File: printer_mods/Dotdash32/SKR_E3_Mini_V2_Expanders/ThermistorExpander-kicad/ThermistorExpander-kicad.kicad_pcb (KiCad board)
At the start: 2 copper layers, 20.5 x 21.8 mm, 8 parts, among them J1 SPI_Header, J2 JST-XH2, J3 JST-XH2, J4 JST-XH2

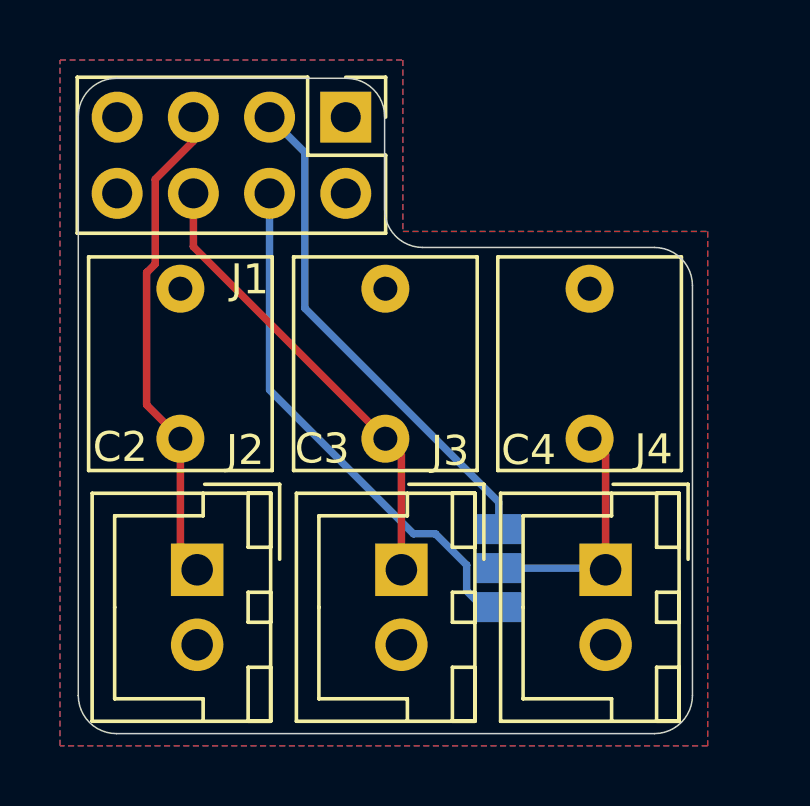
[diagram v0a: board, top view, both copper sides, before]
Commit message: feat: move to SMD capacitors for sourcing
upsetti spaghetti, THT capacitors are hard to find, so we'll just
use SMD (1206) capacitors
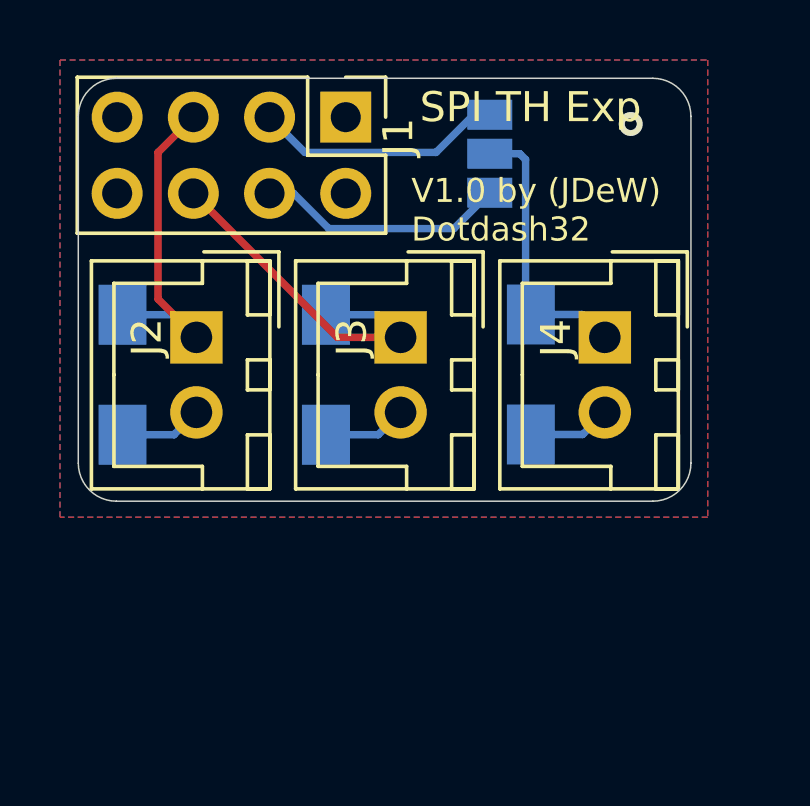
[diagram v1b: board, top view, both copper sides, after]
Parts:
- C2, C3, C4: footprint Capacitors_THT:C_Rect_L7.0mm_W6.0mm_P5.00mm -> Capacitors_SMD:C_1206_HandSoldering; moved to B.Cu
- moved JP1 13.8 mm to (133.1, 76.1)
- moved J2 7.75 mm to (123.3, 82.3)
- moved J3 7.75 mm to (130.1, 82.3)
- moved J4 7.75 mm to (136.9, 82.3)
- moved C3 2.91 mm to (127.6, 83.5), turned to 270 degrees
- moved C4 2.90 mm to (134.4, 83.5), turned to 270 degrees
- moved C2 2.88 mm to (120.8, 83.5), turned to 270 degrees
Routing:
- net /V3.0: track 17.7 -> 8.32 mm
- net /V2.0: track 16.9 -> 8.35 mm
- net GND: track 0.00 -> 8.34 mm, vias 0 -> 1
- net /TH2: track 16.4 -> 11.2 mm
- net /TH3: track 15.4 -> 11.8 mm
- net /TH4: track 8.17 -> 10.0 mm
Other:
- board size 20.5 x 21.8 mm -> 20.4 x 14.1 mm
- board text added: "SPI TH Exp"
- board text added: "V1.0 by (JDeW) Dotdash32"
- board text removed: "SPI TH Exp V1.0 by Dotdash32 (JDeW)"

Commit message: feat: updating BOM, add fiducials
JLCPCB 1206 caps are "discontinued" so moving to instock 0805
capacitors.  Updating BOM, creating LCSC importer
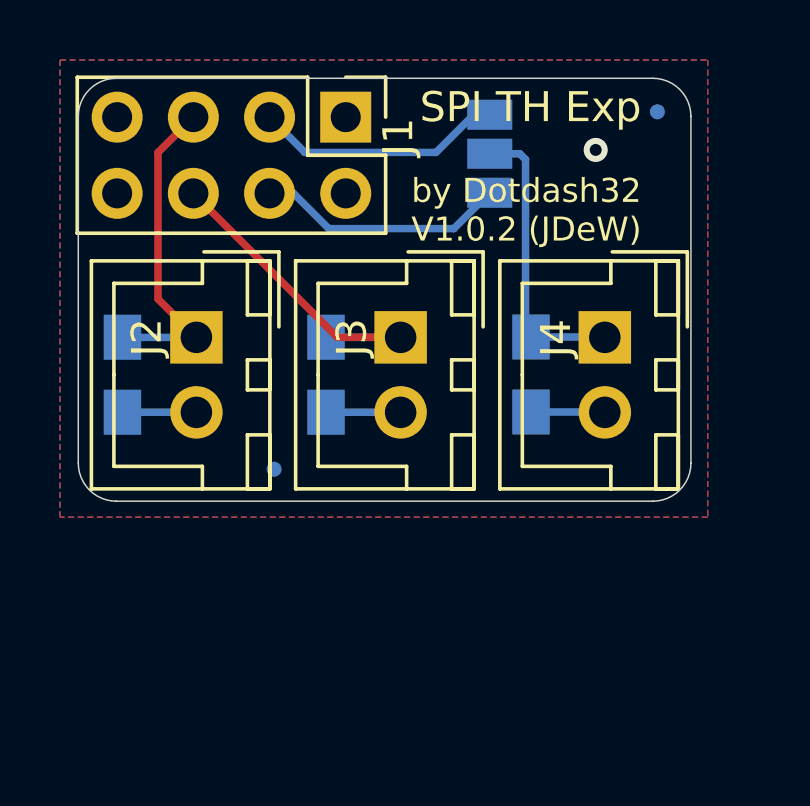
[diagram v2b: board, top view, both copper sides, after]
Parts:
- added FID1: Fiducial, Fiducials:Fiducial_0.5mm_Dia_1mm_Outer, B.Cu at (125.9, 86.7)
- added FID2: Fiducial, Fiducials:Fiducial_0.5mm_Dia_1mm_Outer, B.Cu at (138.7, 74.8)
- C2, C3, C4: footprint Capacitors_SMD:C_1206_HandSoldering -> Capacitors_SMD:C_0805_HandSoldering
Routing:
- net GND: track 8.34 -> 7.43 mm
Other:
- board text added: "by Dotdash32 V1.0.2 (JDeW)"
- board text removed: "V1.0 by (JDeW) Dotdash32"

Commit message: chore: update Thermistor expander to KiCad 6
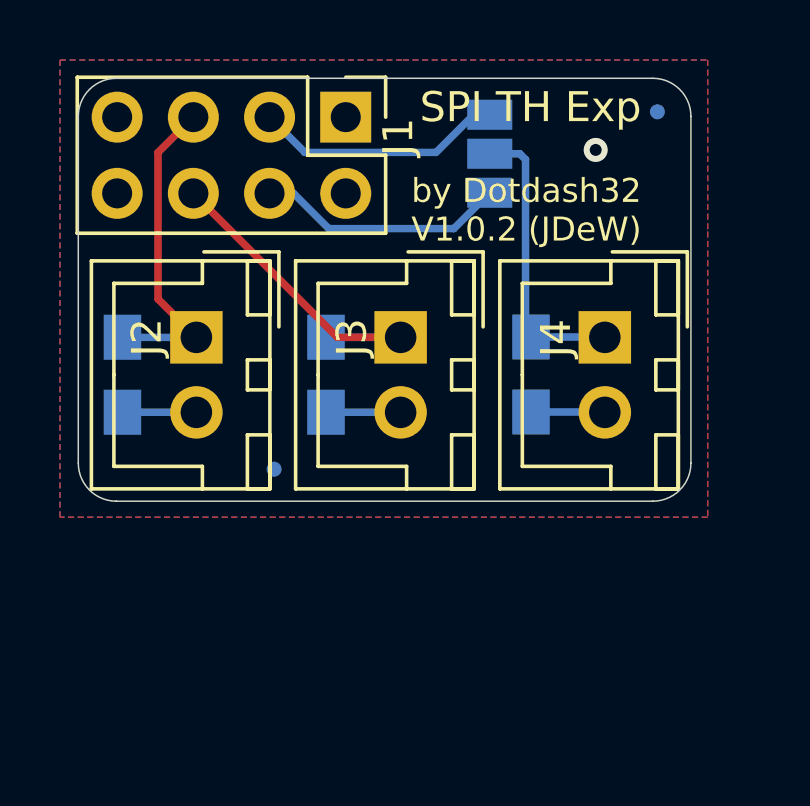
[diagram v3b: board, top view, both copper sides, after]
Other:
- net class Default removed
